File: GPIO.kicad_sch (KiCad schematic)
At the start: 26 parts, among them J11 74LS245, J9 uPD446, K15 74LS04, U1 74LS245, U2 74LS10

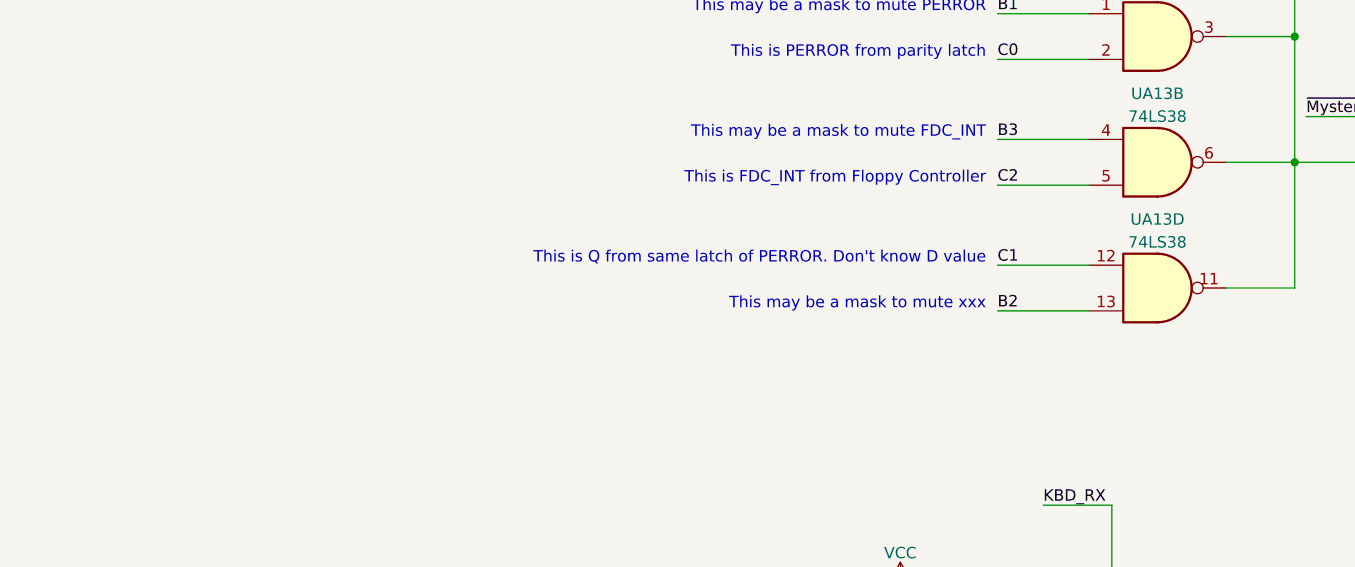
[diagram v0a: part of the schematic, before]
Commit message: Found vsync frame signal for z80 + minors
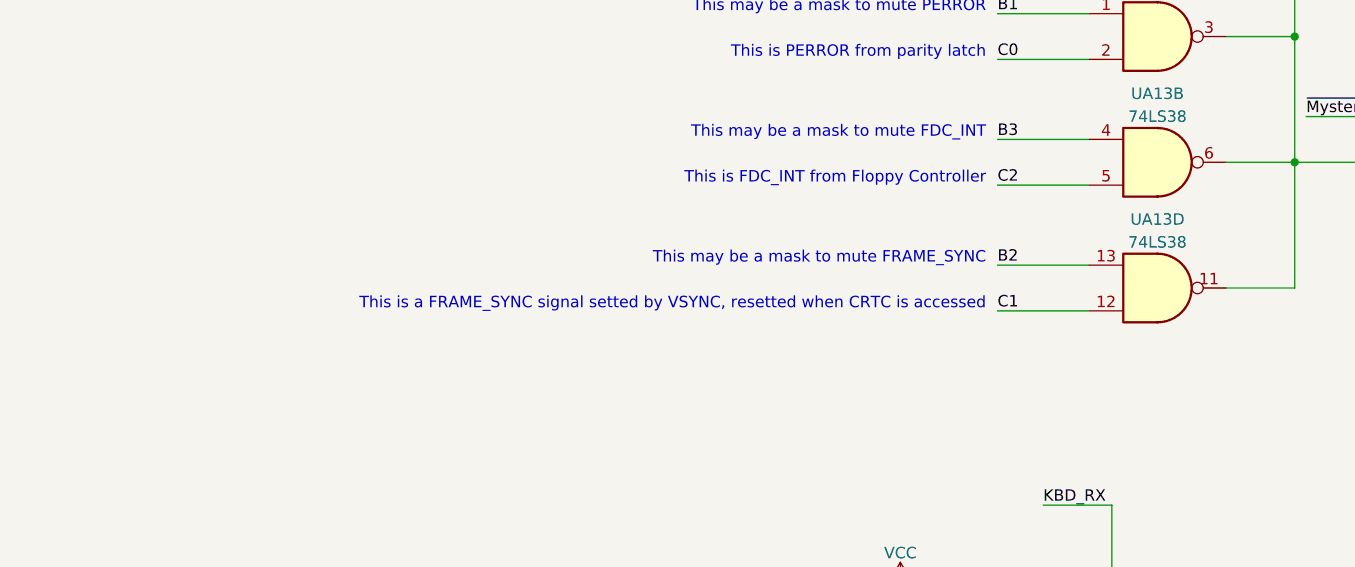
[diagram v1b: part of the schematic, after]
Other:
- note added: "This is a FRAME_SYNC signal setted by VSYNC, resetted when CRTC is accessed"
- note added: "This may be a mask to mute FRAME_SYNC"
- note removed: "This is Q from same latch of PERROR. Don't know D value"
- note removed: "This may be a mask to mute xxx"

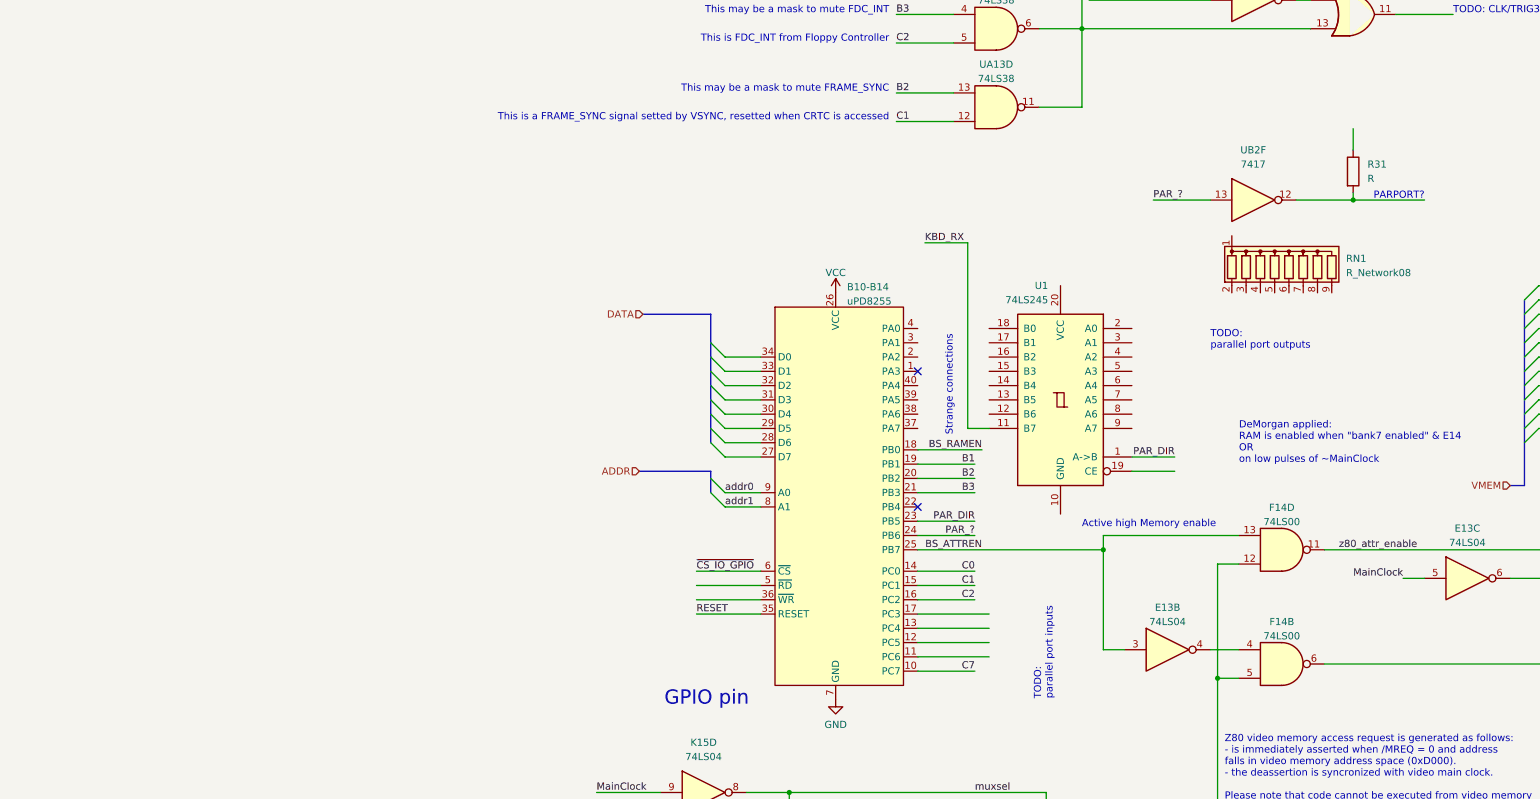
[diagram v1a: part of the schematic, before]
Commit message: parallel port, which is absolutely not a centronics port
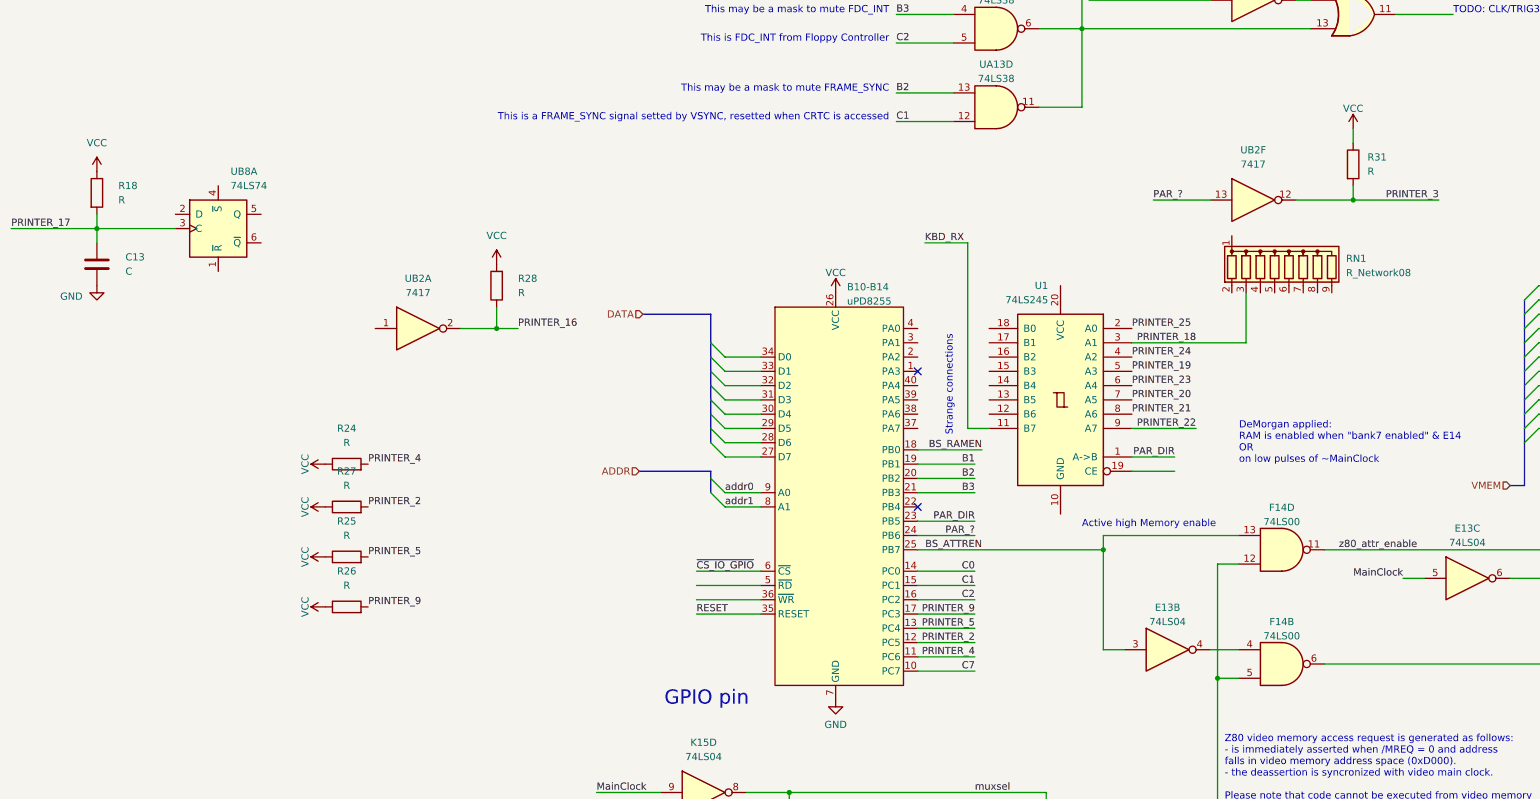
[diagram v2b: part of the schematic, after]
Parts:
- added C13: C, symbol Device:C
- added R18, R24, R25, R26, R27, R28: R, symbol Device:R
- added unit 1 of UB2
- added UB8: 74LS74, symbol 74xx:74LS74
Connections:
- net GND: now also C13.2
- net VCC: now also R31.1, R18.1, R24.1, R25.1, R26.1, R27.1, R28.2
- net PRINTER_3: now reaches R31.2, UB2.12
- net PRINTER_18: now reaches RN1.3 (R2)
- net PRINTER_18: now also U1.3 (A1)
- net PRINTER_4: now reaches B10-B14.11 (PC6)
- net PRINTER_4: now also R24.2
- net PRINTER_2: now reaches B10-B14.12 (PC5)
- net PRINTER_2: now also R27.2
- net PRINTER_5: now reaches B10-B14.13 (PC4)
- net PRINTER_5: now also R25.2
- net PRINTER_9: now reaches B10-B14.17 (PC3)
- net PRINTER_9: now also R26.2
- net PRINTER_25: now reaches U1.2 (A0)
- net PRINTER_24: now reaches U1.4 (A2)
- net PRINTER_19: now reaches U1.5 (A3)
- net PRINTER_23: now reaches U1.6 (A4)
- net PRINTER_20: now reaches U1.7 (A5)
- net PRINTER_21: now reaches U1.8 (A6)
- net PRINTER_22: now reaches U1.9 (A7)
- new net PRINTER_16: R28.1, UB2.2
- new net PRINTER_17: C13.1, R18.2, UB8.3 (C)
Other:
- note removed: "PARPORT?"
- note removed: "TODO: parallel port inputs"
- note removed: "TODO: parallel port outputs"
- moved on the sheet: R31

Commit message: CTC, serial clock and main clock
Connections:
- net PRINTER_19: now also RN1.5 (R4)
- net PRINTER_20: now also RN1.7 (R6)
- net PRINTER_21: now also RN1.8 (R7)
- net PRINTER_22: now also RN1.9 (R8)
- net PRINTER_23: now also RN1.6 (R5)
- net PRINTER_24: now also RN1.4 (R3)
- net PRINTER_25: now also RN1.2 (R1)
- net ~{RD}: now also B10-B14.5 (~{RD})
- net ~{WR}: now also B10-B14.36 (~{WR})
- net TRIG3: now reaches UE16.11
- net B4: now reaches B10-B14.22 (PB4)
- no-connect marks 2 -> 1
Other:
- note added: "GND?"
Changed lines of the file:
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@@
   )
   (no_connect (at 69.85 49.53))
-  (no_connect (at 69.85 73.66))
   (bus_entry (at 271.78 62.23) (size 2.54 2.54)
     (stroke (width 0) (type default))
@@
     (stroke (width 0) (type default))
   )
-  (wire (pts (xy 119.38 59.69) (xy 107.95 59.69))
+  (wire (pts (xy 107.95 59.69) (xy 143.51 59.69))
     (stroke (width 0) (type default))
   )
@@
     (stroke (width 0) (type default))
   )
+  (wire (pts (xy 107.95 41.91) (xy 125.73 41.91))
+    (stroke (width 0) (type default))
+  )
   (wire (pts (xy 234.95 49.53) (xy 238.76 49.53))
     (stroke (width 0) (type default))
@@
     (stroke (width 0) (type default))
   )
+  (wire (pts (xy 125.73 41.91) (xy 125.73 35.56))
+    (stroke (width 0) (type default))
+  )
   (wire (pts (xy -46.99 142.24) (xy -38.1 142.24))
     (stroke (width 0) (type default))
@@
     (stroke (width 0) (type default))
   )
+  (wire (pts (xy 107.95 52.07) (xy 135.89 52.07))
+    (stroke (width 0) (type default))
+  )
   (wire (pts (xy 127 104.14) (xy 123.19 104.14))
     (stroke (width 0) (type default))
@@
     (stroke (width 0) (type default))
   )
+  (wire (pts (xy 138.43 54.61) (xy 138.43 35.56))
+    (stroke (width 0) (type default))
+  )
   (bus (pts (xy 132.08 228.6) (xy 132.08 231.14))
     (stroke (width 0) (type default))
@@
     (stroke (width 0) (type default))
   )
+  (wire (pts (xy 130.81 46.99) (xy 130.81 35.56))
+    (stroke (width 0) (type default))
+  )
   (wire (pts (xy -7.62 274.32) (xy -7.62 270.51))
     (stroke (width 0) (type default))
@@
     (stroke (width 0) (type default))
   )
+  (wire (pts (xy 133.35 35.56) (xy 133.35 49.53))
+    (stroke (width 0) (type default))
+  )
   (wire (pts (xy 66.04 157.48) (xy 66.04 151.13))
     (stroke (width 0) (type default))
@@
     (stroke (width 0) (type default))
   )
+  (wire (pts (xy 107.95 57.15) (xy 140.97 57.15))
+    (stroke (width 0) (type default))
+  )
   (bus (pts (xy 33.02 39.37) (xy 20.955 39.37))
     (stroke (width 0) (type default))
@@
     (stroke (width 0) (type default))
   )
+  (wire (pts (xy 133.35 49.53) (xy 107.95 49.53))
+    (stroke (width 0) (type default))
+  )
   (bus (pts (xy 132.08 290.83) (xy 132.08 294.64))
     (stroke (width 0) (type default))
@@
     (stroke (width 0) (type default))
   )
+  (wire (pts (xy 107.95 46.99) (xy 130.81 46.99))
+    (stroke (width 0) (type default))
+  )
   (wire (pts (xy 107.95 64.77) (xy 115.57 64.77))
     (stroke (width 0) (type default))
@@
     (stroke (width 0) (type default))
   )
+  (wire (pts (xy 143.51 59.69) (xy 143.51 35.56))
+    (stroke (width 0) (type default))
+  )
   (wire (pts (xy 73.66 162.56) (xy 82.55 162.56))
     (stroke (width 0) (type default))
@@
     (stroke (width 0) (type default))
   )
+  (wire (pts (xy 135.89 52.07) (xy 135.89 35.56))
+    (stroke (width 0) (type default))
+  )
   (wire (pts (xy 74.93 226.06) (xy 88.9 226.06))
     (stroke (width 0) (type default))
@@
     (stroke (width 0) (type default))
   )
+  (wire (pts (xy 107.95 54.61) (xy 138.43 54.61))
+    (stroke (width 0) (type default))
+  )
   (wire (pts (xy 91.44 -25.4) (xy 99.06 -25.4))
     (stroke (width 0) (type default))
@@
     (stroke (width 0) (type default))
   )
+  (wire (pts (xy 140.97 57.15) (xy 140.97 35.56))
+    (stroke (width 0) (type default))
+  )
   (wire (pts (xy 121.92 19.05) (xy 111.76 19.05))
     (stroke (width 0) (type default))
@@
   )
   (wire (pts (xy 73.66 151.13) (xy 66.04 151.13))
+    (stroke (width 0) (type default))
+  )
+  (wire (pts (xy 69.85 73.66) (xy 80.01 73.66))
     (stroke (width 0) (type default))
   )
@@
     (effects (font (size 1.27 1.27)) (justify right bottom))
   )
+  (text "GND?" (at 116.84 68.58 0)
+    (effects (font (size 1.27 1.27)) (justify left bottom))
+  )
   (text "TODO" (at 21.59 280.67 0)
     (effects (font (size 1.27 1.27)) (justify right bottom))
@@
     (effects (font (size 1.27 1.27)) (justify right bottom))
   )
+  (label "~{WR}" (at 30.48 90.17 0) (fields_autoplaced)
+    (effects (font (size 1.27 1.27)) (justify left bottom))
+  )
   (label "vmem_oe" (at 21.59 293.37 180) (fields_autoplaced)
     (effects (font (size 1.27 1.27)) (justify right bottom))
@@
     (effects (font (size 1.27 1.27)) (justify right bottom))
   )
+  (label "TRIG3" (at 165.1 -13.97 180) (fields_autoplaced)
+    (effects (font (size 1.27 1.27)) (justify right bottom))
+  )
   (label "~{MysteriousTrigger_CS}" (at 100.33 -16.51 0) (fields_autoplaced)
     (effects (font (size 1.27 1.27)) (justify left bottom))
@@
     (effects (font (size 1.27 1.27)) (justify left bottom))
   )
+  (label "B4" (at 80.01 73.66 180) (fields_autoplaced)
+    (effects (font (size 1.27 1.27)) (justify right bottom))
+  )
   (label "vmem_oniric" (at -19.05 274.32 0) (fields_autoplaced)
     (effects (font (size 1.27 1.27)) (justify left bottom))
@@
     (effects (font (size 1.27 1.27)) (justify left bottom))
   )
+  (label "~{RD}" (at 30.48 87.63 0) (fields_autoplaced)
+    (effects (font (size 1.27 1.27)) (justify left bottom))
+  )
